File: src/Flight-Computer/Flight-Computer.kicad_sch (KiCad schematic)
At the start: 41 parts, among them J1 Jumper_NO, P1 282837-2, P2 647676-2, P8 3220-20-0200-00, U1 STM32H750VBTx, U2 LMS8117AMP-3.3_NOPB, Y1 ECS-240-18-33-JGN-TR

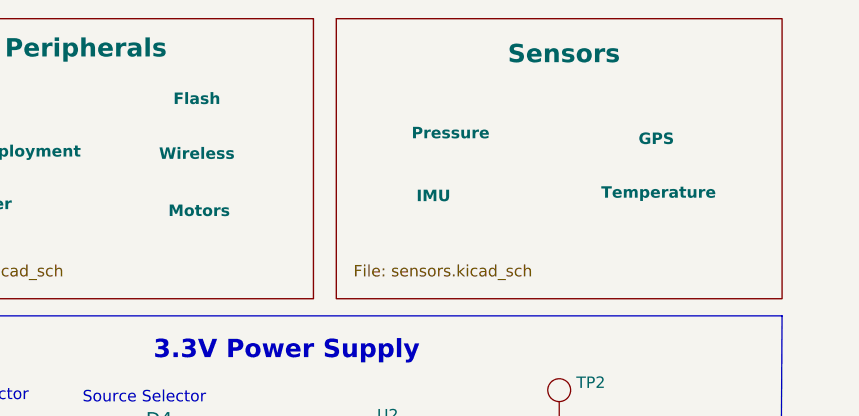
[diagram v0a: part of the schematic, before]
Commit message: minor schematic formatting changes
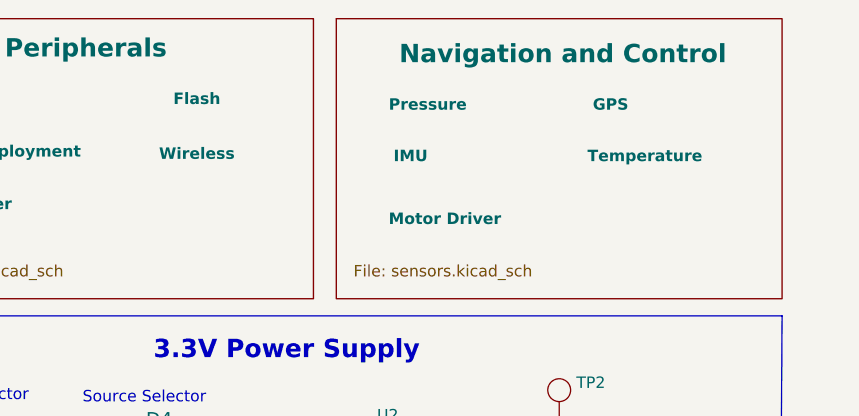
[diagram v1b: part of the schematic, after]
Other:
- sheet Sensors renamed Navigation and Control
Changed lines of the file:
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@@
     (stroke (width 0.1524) (type solid) (color 0 0 0 0))
     (fill (color 0 0 0 0.0000))
-    (property "Sheet name" "Sensors" (id 0) (at 251.46 24.13 0)
+    (property "Sheet name" "Navigation and Control" (id 0) (at 239.395 24.13 0)
       (effects (font (size 2.032 2.032) bold) (justify left bottom))
     )
@@
       (effects (font (size 1.27 1.27)) (justify left top))
     )
-    (property "Field2" "IMU" (id 2) (at 243.205 38.735 0)
+    (property "Field2" "IMU" (id 2) (at 240.665 34.29 0)
       (effects (font (size 1.27 1.27) bold))
     )
-    (property "Field3" "GPS" (id 3) (at 267.97 32.385 0)
+    (property "Field3" "GPS" (id 3) (at 262.89 28.575 0)
       (effects (font (size 1.27 1.27) bold))
     )
-    (property "Field4" "Pressure" (id 4) (at 245.11 31.75 0)
+    (property "Field4" "Pressure" (id 4) (at 242.57 28.575 0)
       (effects (font (size 1.27 1.27) bold))
     )
-    (property "Field5" "Temperature" (id 5) (at 268.224 38.354 0)
+    (property "Field5" "Temperature" (id 5) (at 266.7 34.29 0)
+      (effects (font (size 1.27 1.27) bold))
+    )
+    (property "Field6" "Motor Driver" (id 6) (at 244.475 41.275 0)
       (effects (font (size 1.27 1.27) bold))
     )
@@
       (effects (font (size 1.27 1.27) bold))
     )
-    (property "Field7" "Motors" (id 7) (at 217.17 40.386 0)
-      (effects (font (size 1.27 1.27) bold))
-    )

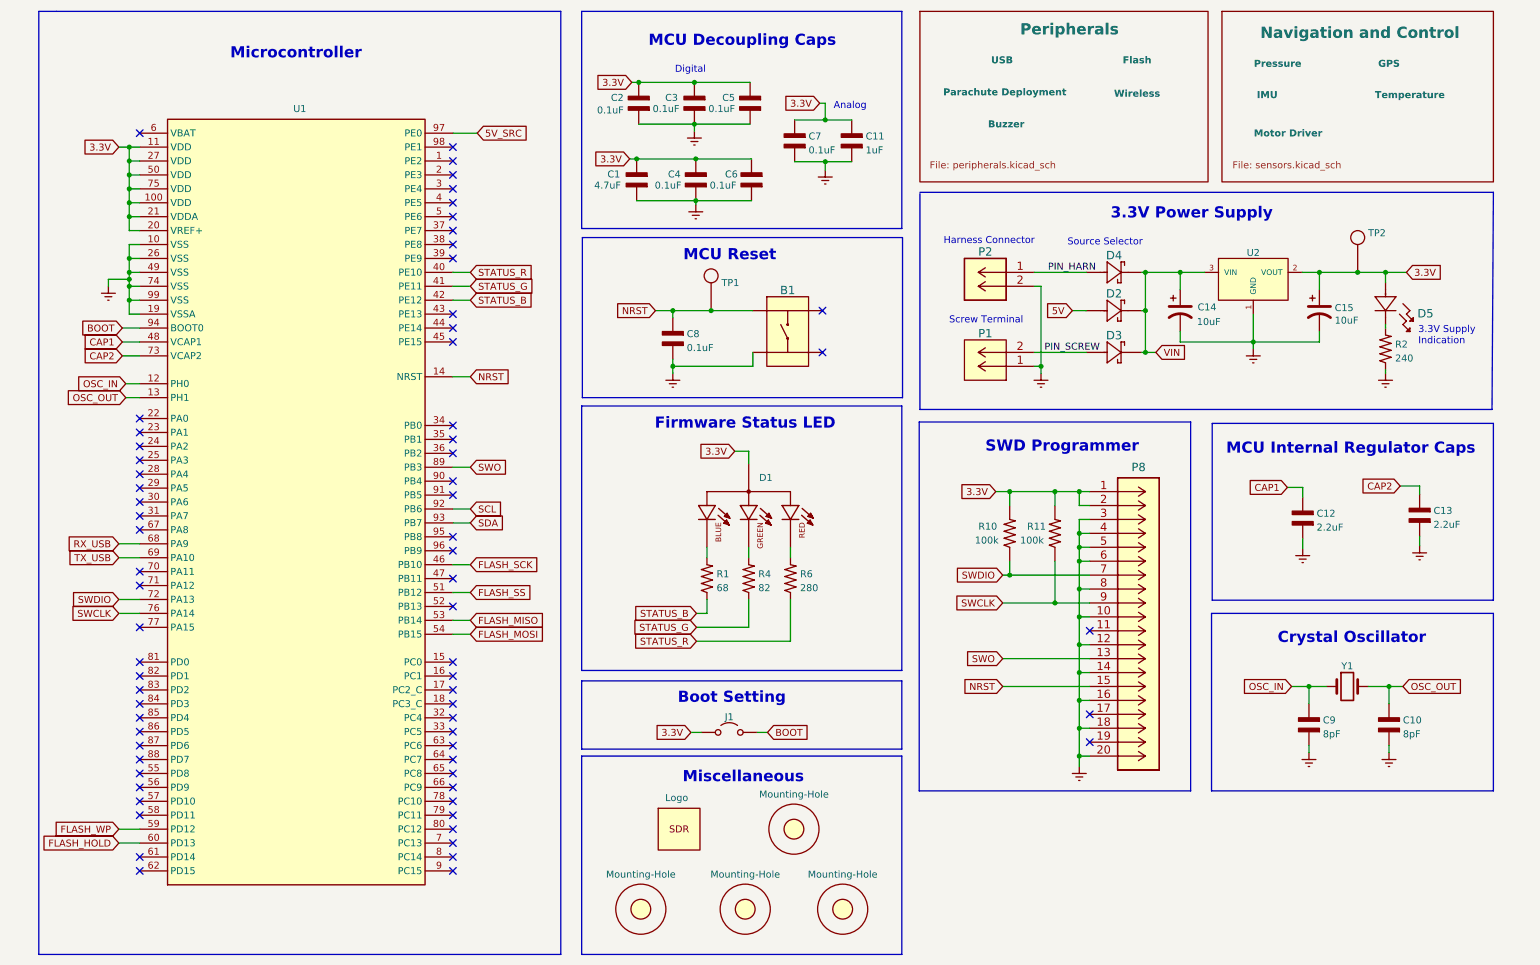
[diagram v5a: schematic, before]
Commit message: added mcu signals for peripherals
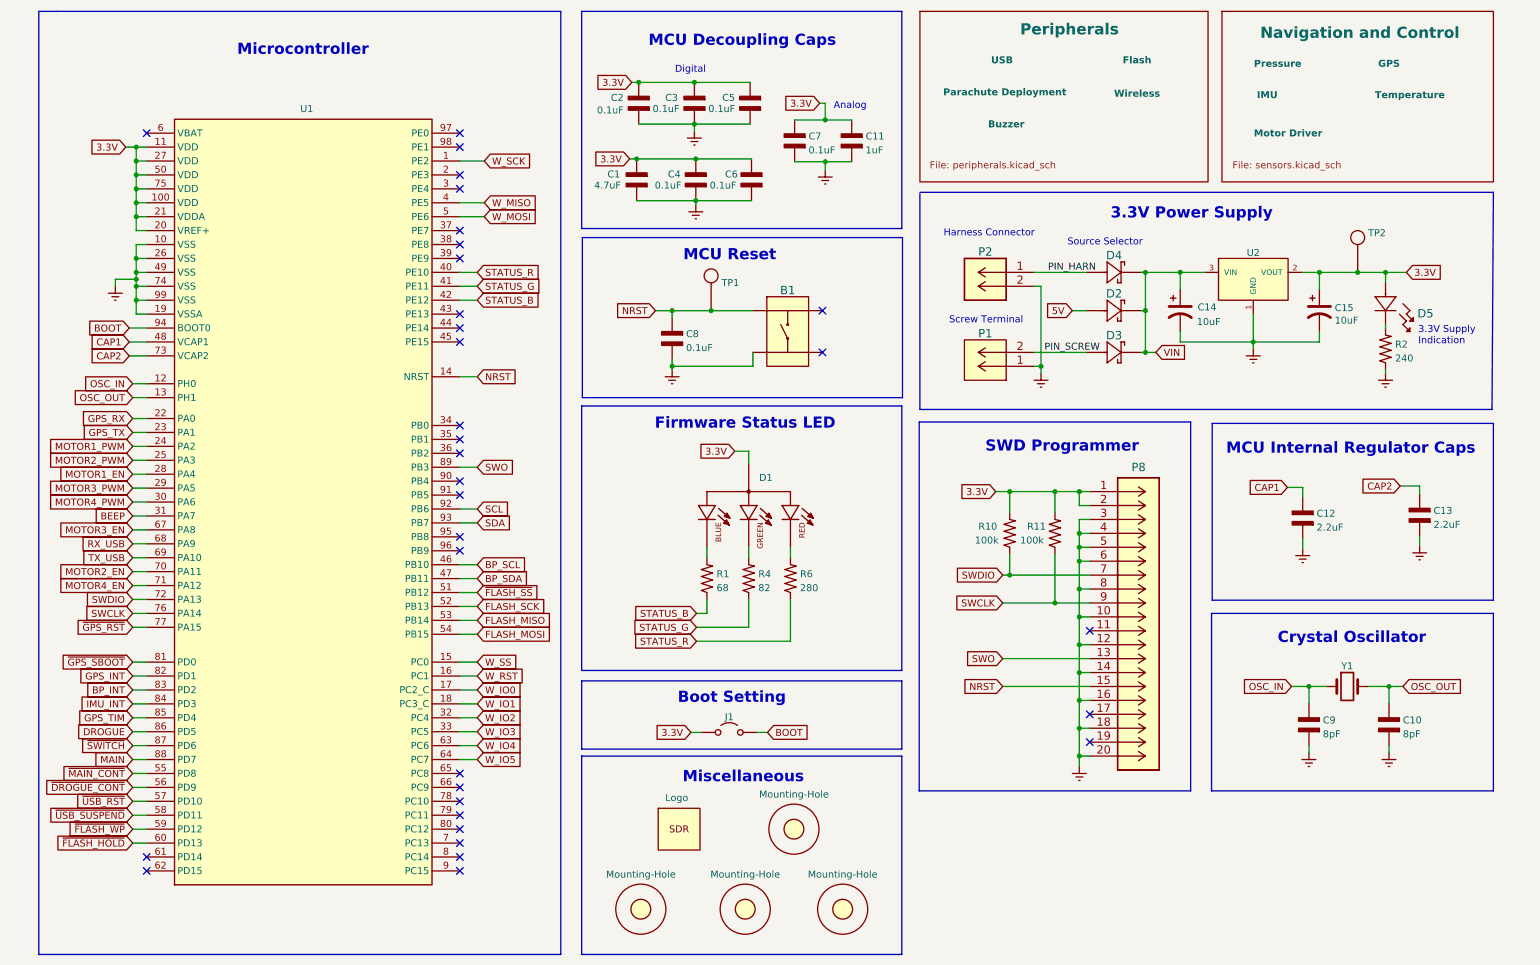
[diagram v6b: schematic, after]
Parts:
- B1: footprint SW_PTS647SM38SMTR2LFS_CNK -> Flight-Computer:PTS647SM38SMTR2LFS
- C1, C10, C11, C12, C13, C14, C15, C2, C3, C4, C5, C6, C7, C8, C9: footprint (none) -> Flight-Computer:CAP_0603
- D1: footprint LED_CLMVC-FKA-CL1D1L71BB7C3C3 -> Flight-Computer:CLMVC-FKA-CL1D1L71BB7C3C3
- D2, D3, D4: footprint SOD-123FL_MCC -> Flight-Computer:SM5819PL-TP
- D5: footprint (none) -> Flight-Computer:SML-LX1206GC-TR
- H1, H2, H3, H4: footprint (none) -> Flight-Computer:MountingHole_4.3mm_M4_DIN965
- J1: footprint (none) -> Flight-Computer:Jumper-NO
- LOGO1: footprint (none) -> Flight-Computer:Logo
- P1: footprint 66953-005LF_AMP -> Flight-Computer:282837-2
- P2: footprint CONN_2043-1X04G00DAU_OUP -> Flight-Computer:282837-6
- P8: footprint CONN20_D10-RA-BK_SUL -> Flight-Computer:3220-20-0200-00
- R1, R10, R11, R2, R4, R6: footprint (none) -> Flight-Computer:RES_0603
- TP1, TP2: footprint (none) -> Flight-Computer:TP
- U1: footprint Package_QFP:LQFP-100_14x14mm_P0.5mm -> Flight-Computer:STM32H750VBT6; symbol Flight-Computer-rescue:STM32H750VBTx-Engine-Controller -> Flight-Computer:STM32H750VBTx
- U2: footprint (none) -> Flight-Computer:LMS8117AMP-3.3NOPB
- Y1: footprint (none) -> Flight-Computer:ECS-240-18-33-JGN-TR
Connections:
- net FLASH_SCK: now also U1.52 (PB13); no longer U1.46 (PB10)
- net W_SCK: now reaches U1.1 (PE2)
- net W_SS: now reaches U1.15 (PC0)
- net W_RST: now reaches U1.16 (PC1)
- net W_IO0: now reaches U1.17 (PC2_C)
- net W_IO1: now reaches U1.18 (PC3_C)
- net GPS_RX: now reaches U1.22 (PA0)
- net GPS_TX: now reaches U1.23 (PA1)
- net MOTOR1_PWM: now reaches U1.24 (PA2)
- net MOTOR2_PWM: now reaches U1.25 (PA3)
- net MOTOR1_EN: now reaches U1.28 (PA4)
- net MOTOR3_PWM: now reaches U1.29 (PA5)
- net MOTOR4_PWM: now reaches U1.30 (PA6)
- net BEEP: now reaches U1.31 (PA7)
- net W_IO2: now reaches U1.32 (PC4)
- net W_IO3: now reaches U1.33 (PC5)
- net W_MISO: now reaches U1.4 (PE5)
- net BP_SDA: now reaches U1.47 (PB11)
- net W_MOSI: now reaches U1.5 (PE6)
- net ~{MAIN_CONT}: now reaches U1.55 (PD8)
- net ~{DROGUE_CONT}: now reaches U1.56 (PD9)
- net ~{USB_RST}: now reaches U1.57 (PD10)
- net ~{USB_SUSPEND}: now reaches U1.58 (PD11)
- net W_IO4: now reaches U1.63 (PC6)
- net W_IO5: now reaches U1.64 (PC7)
- net MOTOR3_EN: now reaches U1.67 (PA8)
- net MOTOR2_EN: now reaches U1.70 (PA11)
- net MOTOR4_EN: now reaches U1.71 (PA12)
- net ~{GPS_RST}: now reaches U1.77 (PA15)
- net ~{GPS_SBOOT}: now reaches U1.81 (PD0)
- net GPS_INT: now reaches U1.82 (PD1)
- net BP_INT: now reaches U1.83 (PD2)
- net IMU_INT: now reaches U1.84 (PD3)
- net GPS_TIM: now reaches U1.85 (PD4)
- net DROGUE: now reaches U1.86 (PD5)
- net ~{SWITCH}: now reaches U1.87 (PD6)
- net MAIN: now reaches U1.88 (PD7)
- net 5V_SRC: no longer names the net of U1.97 (PE0)
- net FLASH_HOLD renamed ~{FLASH_HOLD}
- net FLASH_SS renamed ~{FLASH_SS}
- net FLASH_WP renamed ~{FLASH_WP}
- new net BP_SCL: U1.46 (PB10)
- no-connect marks 69 -> 33
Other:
- moved on the sheet: U1

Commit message: setup layout design rules
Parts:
- P2: footprint Flight-Computer:282837-6 -> Flight-Computer:647676-2
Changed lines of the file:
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@@
     )
     (pin "1")
+    (pin "2")
     (pin "3")
+    (pin "4")
   )
   (symbol (lib_id "Flight-Computer:CAP_0603") (at 146.558 49.784 90) (unit 1)
@@
       (effects (font (size 1.524 1.524)) hide)
     )
-    (property "Footprint" "Flight-Computer:282837-6" (id 2) (at 189.23 80.645 0)
+    (property "Footprint" "Flight-Computer:647676-2" (id 2) (at 189.23 80.645 0)
       (effects (font (size 1.524 1.524)) hide)
     )
@@
     )
     (path "/e6b0a6aa-1b72-4f34-b466-8560e486da99"
-      (reference "P2") (unit 1) (value "647676-2") (footprint "Flight-Computer:282837-6")
+      (reference "P2") (unit 1) (value "647676-2") (footprint "Flight-Computer:647676-2")
     )
     (path "/b65729ce-aade-4707-9cc1-eb9bb9e47e4f/cba84471-3533-47a7-8ab9-8b3ef15eb4c6"
@@
     )
     (path "/b65729ce-aade-4707-9cc1-eb9bb9e47e4f/0ad4323c-4eaa-404c-9547-e0e8fb3a71f4"
-      (reference "Q1") (unit 1) (value "QS5U17TR") (footprint "Package_TO_SOT_THT:TO-92_Inline")
+      (reference "Q1") (unit 1) (value "QS5U17TR") (footprint "Engine-Controller:QS5U17TR")
     )
     (path "/b65729ce-aade-4707-9cc1-eb9bb9e47e4f/fe1a29a9-92fa-44e3-a65d-df1bddd585be"
-      (reference "Q2") (unit 1) (value "QS5U17TR") (footprint "Package_TO_SOT_THT:TO-92_Inline")
+      (reference "Q2") (unit 1) (value "QS5U17TR") (footprint "Engine-Controller:QS5U17TR")
     )
     (path "/a7215684-cee9-4aba-87f1-e5962f77da19/20a8364e-675c-422e-8961-8b47c055f930"
-      (reference "Q3") (unit 1) (value "QS5U17TR") (footprint "Package_TO_SOT_THT:TO-92_Inline")
+      (reference "Q3") (unit 1) (value "QS5U17TR") (footprint "Engine-Controller:QS5U17TR")
     )
     (path "/a7215684-cee9-4aba-87f1-e5962f77da19/31a741d5-d576-475a-a567-e94d06aa5a7d"
-      (reference "Q4") (unit 1) (value "QS5U17TR") (footprint "Package_TO_SOT_THT:TO-92_Inline")
+      (reference "Q4") (unit 1) (value "QS5U17TR") (footprint "Engine-Controller:QS5U17TR")
     )
     (path "/a7215684-cee9-4aba-87f1-e5962f77da19/4aecd815-6d57-4a6c-aa4a-51b0fe69fc8a"
-      (reference "Q5") (unit 1) (value "QS5U17TR") (footprint "Package_TO_SOT_THT:TO-92_Inline")
+      (reference "Q5") (unit 1) (value "QS5U17TR") (footprint "Engine-Controller:QS5U17TR")
     )
     (path "/a7215684-cee9-4aba-87f1-e5962f77da19/dfe561ab-157f-4431-9d79-37d61e74ce29"
-      (reference "Q6") (unit 1) (value "QS5U17TR") (footprint "Package_TO_SOT_THT:TO-92_Inline")
+      (reference "Q6") (unit 1) (value "QS5U17TR") (footprint "Engine-Controller:QS5U17TR")
     )
     (path "/c5bc671e-4f2a-47b5-9c00-3f0bc44ffb57"

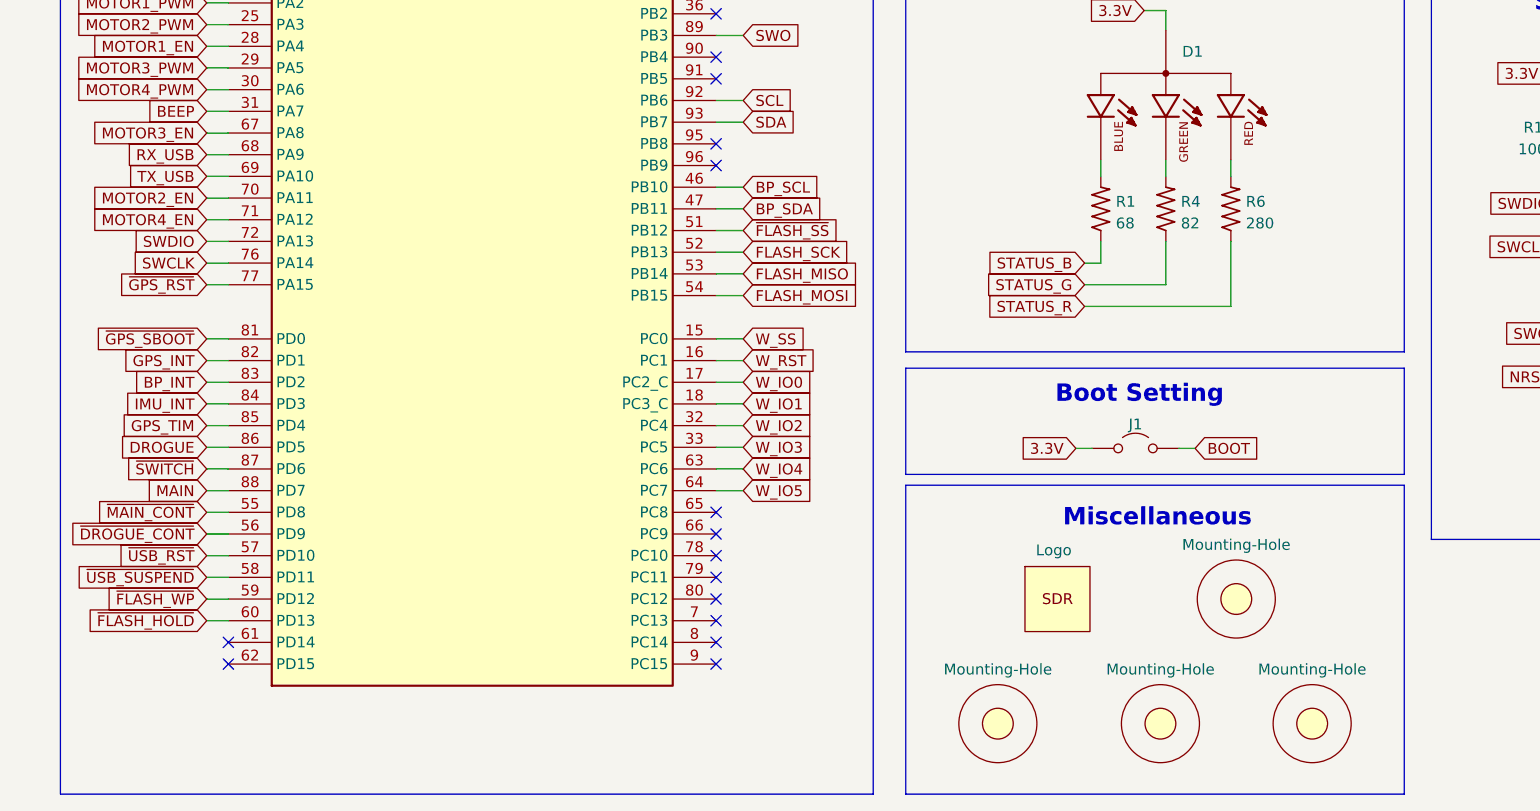
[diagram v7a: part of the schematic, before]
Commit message: placed pcb parts on board and defined form factor
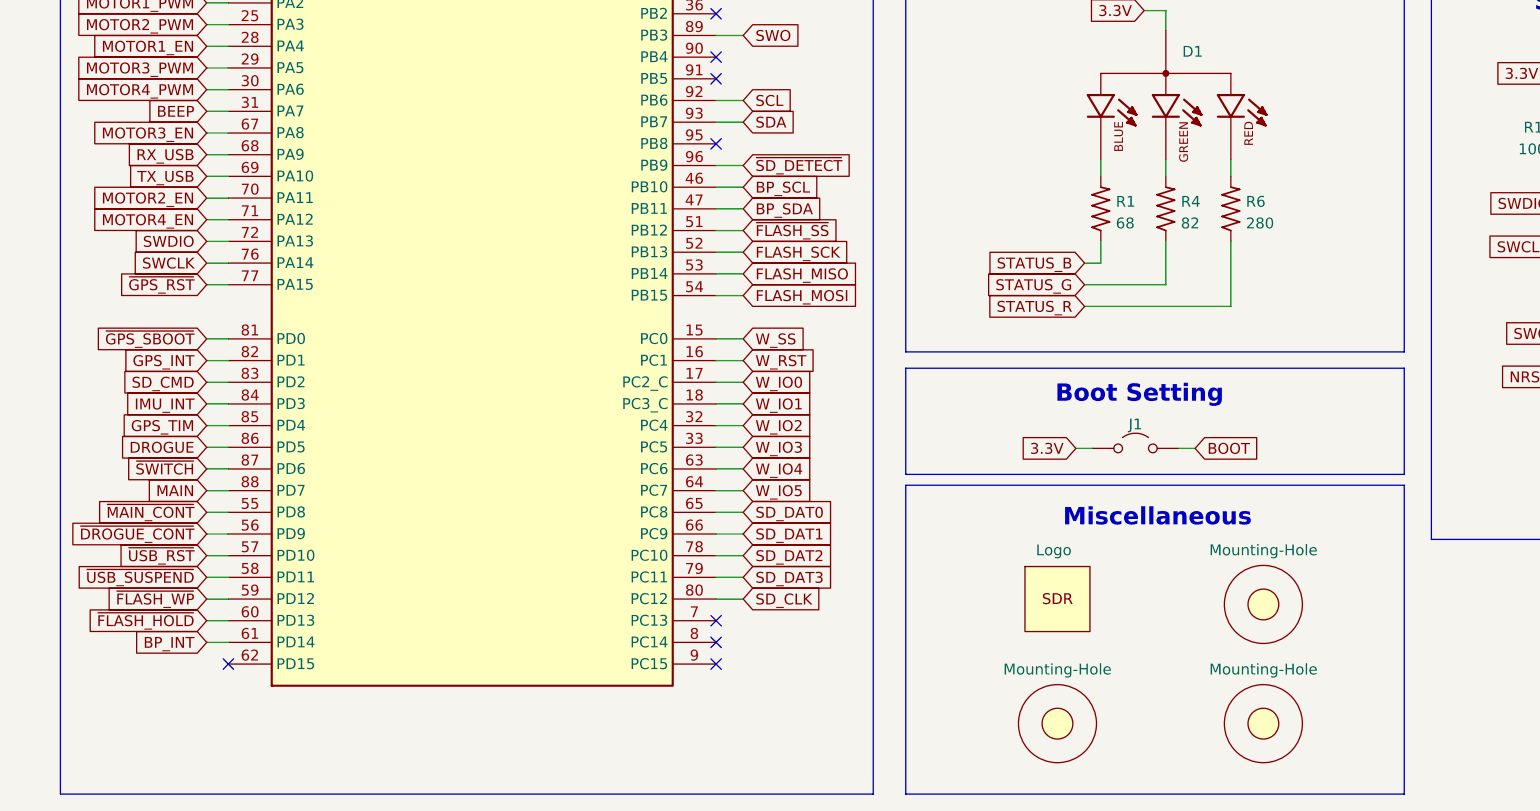
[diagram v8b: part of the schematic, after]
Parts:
- removed H2: Mounting-Hole, Flight-Computer:MountingHole_4.3mm_M4_DIN965, symbol Flight-Computer:Mounting-Hole
- C14, C15: footprint Flight-Computer:CAP_0603 -> Flight-Computer:T491A106K010AT
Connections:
- net BP_INT: now also U1.61 (PD14); no longer U1.83 (PD2)
- net SD_DAT0: now reaches U1.65 (PC8)
- net SD_DAT1: now reaches U1.66 (PC9)
- net SD_DAT2: now reaches U1.78 (PC10)
- net SD_DAT3: now reaches U1.79 (PC11)
- net SD_CLK: now reaches U1.80 (PC12)
- net ~{SD_DETECT}: now reaches U1.96 (PB9)
- new net SD_CMD: U1.83 (PD2)
- no-connect marks 33 -> 26
